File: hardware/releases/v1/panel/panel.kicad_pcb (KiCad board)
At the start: 4 copper layers, 101 x 76.5 mm, 109 parts, among them J1 KNX bus terminal pins, J2 AUX, J3 DALI, J4 JST-SH 1x10, Q1 MJD45H11, Q2 BC857, Q3 IRLML0060, Q4 BC847, Q5 BC847, Q6 BC847, U1 NCN5130MNTWG, U2 SCT2400TVBR, U3 REM3-2415S/A/CTRL 24V->15V 3W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, U4 TLP383, U5 TLP383(D4BLLTL,E, U6 TLP383(D4BLLTL,E, U7 LM66100, U8 XIAO ESP32C6, Y1 16MHz

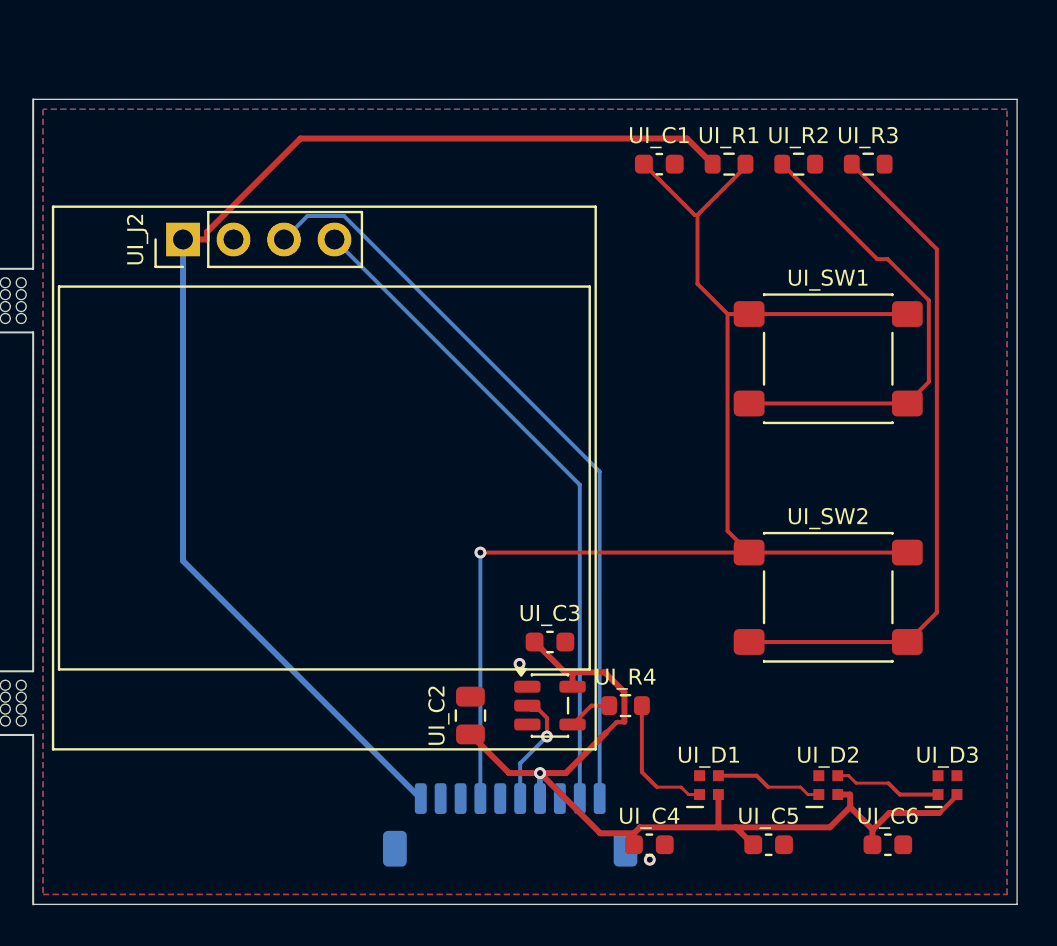
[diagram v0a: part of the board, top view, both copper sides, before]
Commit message: Regenerated V1 hardware release files with updated timestamps and mouse bite footprint reference consolidation
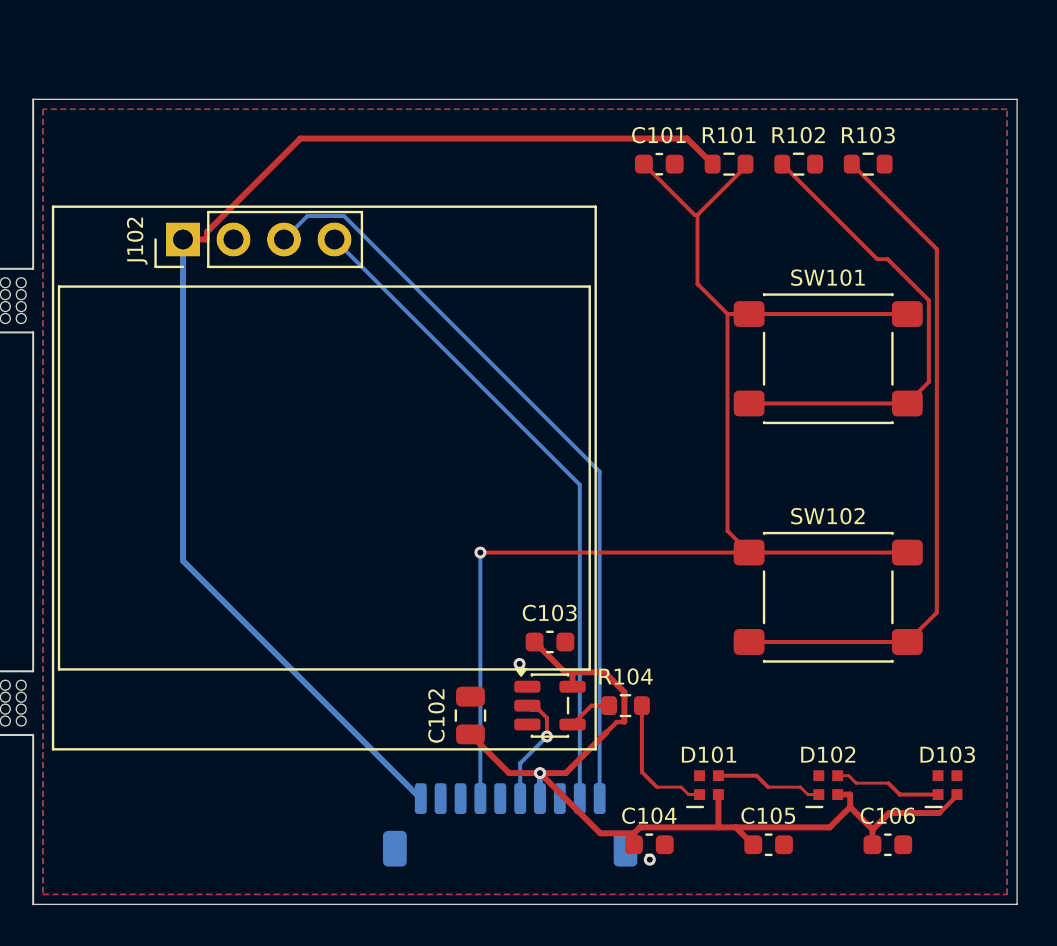
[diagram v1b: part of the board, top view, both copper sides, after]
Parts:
- removed MB1, MB10, MB11, MB12, MB13, MB14, MB15, MB16, MB2, MB3, MB4, MB5, MB6, MB7, MB8, MB9: , 
- added MOUSE_BITES: DNP, , F.Cu at (0.00, 0.00)
- renumbered UI_C1 to C101, UI_C2 to C102, UI_C3 to C103, UI_C4 to C104, UI_C5 to C105, UI_C6 to C106, UI_D1 to D101, UI_D2 to D102, UI_D3 to D103, UI_J1 to J101, UI_J2 to J102, UI_R1 to R101, UI_R2 to R102, UI_R3 to R103, UI_R4 to R104, UI_SW1 to SW101, UI_SW2 to SW102, UI_U1 to U101

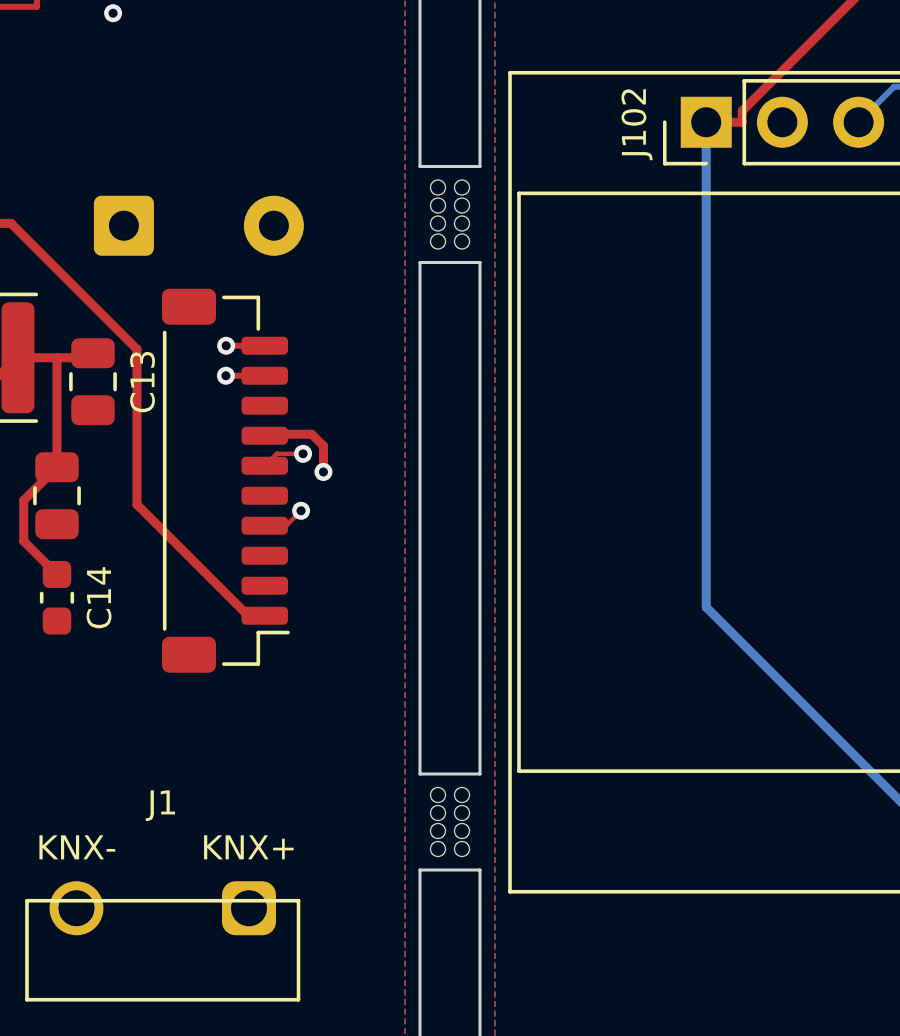
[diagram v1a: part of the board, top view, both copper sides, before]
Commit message: Added custom naming support for channels and groups with persistent storage, D4i power polling during commissioning, and updated web UI to display and edit names in lamp/group tiles and inspector panels
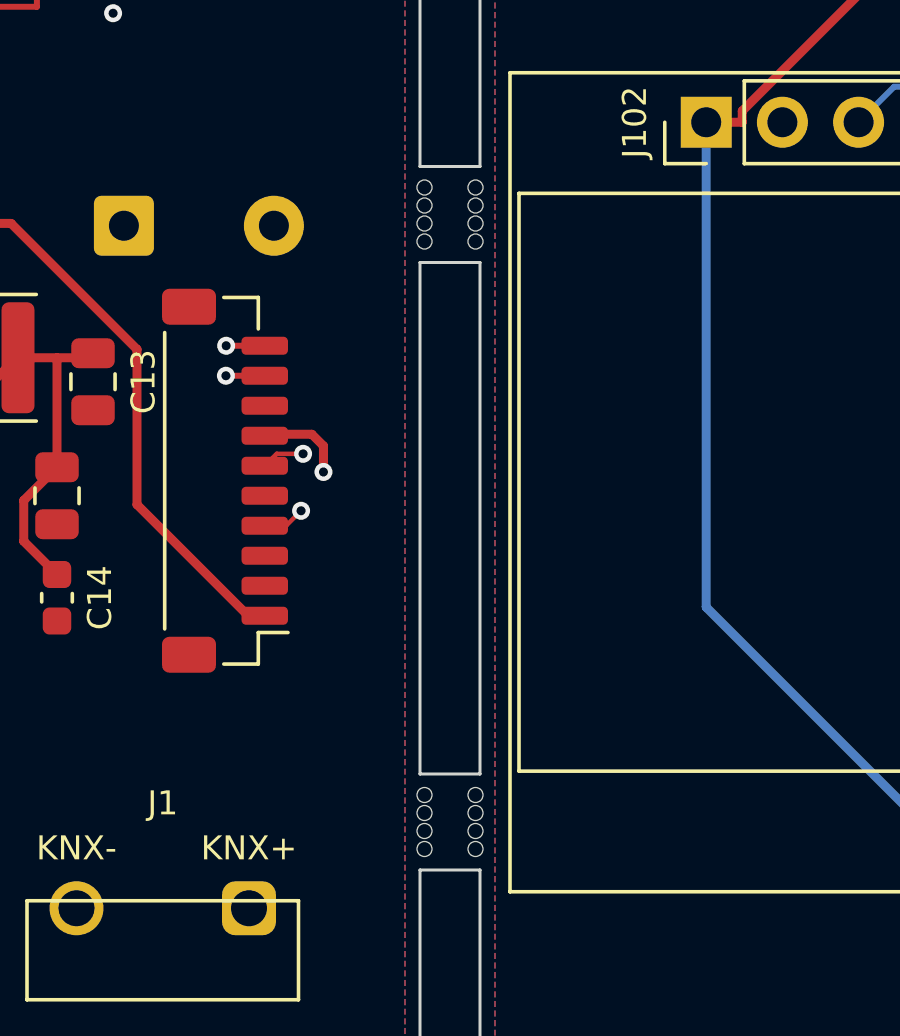
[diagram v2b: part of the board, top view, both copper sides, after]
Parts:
- removed MOUSE_BITES: DNP, 
- added MB1: DNP, , F.Cu at (49.6, -31.3)
- added MB10: DNP, , F.Cu at (51.4, -11.0)
- added MB11: DNP, , F.Cu at (49.6, -10.4)
- added MB12: DNP, , F.Cu at (51.4, -10.4)
- added MB13: DNP, , F.Cu at (49.6, -9.82)
- added MB14: DNP, , F.Cu at (51.4, -9.82)
- added MB15: DNP, , F.Cu at (49.6, -9.22)
- added MB16: DNP, , F.Cu at (51.4, -9.22)
- added MB2: DNP, , F.Cu at (51.4, -31.3)
- added MB3: DNP, , F.Cu at (49.6, -30.7)
- added MB4: DNP, , F.Cu at (51.4, -30.7)
- added MB5: DNP, , F.Cu at (49.6, -30.1)
- added MB6: DNP, , F.Cu at (51.4, -30.1)
- added MB7: DNP, , F.Cu at (49.6, -29.5)
- added MB8: DNP, , F.Cu at (51.4, -29.5)
- added MB9: DNP, , F.Cu at (49.6, -11.0)

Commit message: Updated DALI DC-DC converter from RECOM REM3-2415S/A to REC3-2415SRW/H2/A series across all variants, changed V3 OLED from 14-pin 0.5mm ZIF to 14-pin 0.62mm solder-tail FPC connector, and expanded assembly documentation with Mouser/Digi-Key/TME part numbers and alternative suppliers
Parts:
- U3: value REM3-2415S/A/CTRL 24V->15V 3W iso -> REC3-2415SRW/H2/A/CTRL 24V->15V 3W iso
